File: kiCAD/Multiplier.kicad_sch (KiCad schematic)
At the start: 58 parts, among them IC2 ADG1221BRMZ, J1 Conn_01x02_Pin, J2 Conn_01x02_Pin, J3 Conn_01x02_Pin, Q7 Q_Dual_PNP_PNP_C1B1B2C2E2E1, Q8 Q_Dual_PNP_PNP_C1B1B2C2E2E1, U1 TS912, U10 TPS63060, U2 TLV340, U4 TS912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

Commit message: Initial routing and layout
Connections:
- net VCC: now also Q8.5 (E2); no longer Q7.5 (E2)
- net at Q7.6 (E1), Q8.1 (C1), Q8.2 (B1): now also Q8.3 (B2); no longer Q7.3 (B2)
- net at Q7.4 (C2): now also C1.1, U2.2 (-), U2.6 (-), U7.1; no longer Q8.5 (E2)
- net at Q7.1 (C1), Q7.2 (B1), R5.1: now also Q7.3 (B2); no longer Q8.3 (B2)
- new net: Q7.5 (E2), Q8.4 (C2)
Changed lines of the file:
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@@
-    )
-  )
-  (symbol (lib_id "Device:Q_Dual_PNP_PNP_C1B1B2C2E2E1") (at 76.2 27.94 0) (mirror x) (unit 2)
-    (in_bom yes) (on_board yes) (dnp no)
-    (property "Reference" "Q7" (at 81.28 26.67 0)
-      (effects (font (size 1.27 1.27)) (justify left))
-    )
-    (property "Value" "Q_Dual_PNP_PNP_C1B1B2C2E2E1" (at 81.28 29.21 0)
-      (effects (font (size 1.27 1.27)) (justify left) hide)
-    )
-    (property "Footprint" "Custom:SOT-363_DUAL_PNP" (at 81.28 30.48 0)
-      (effects (font (size 1.27 1.27)) hide)
-    )
-    (property "Datasheet" "https://www.diodes.com/assets/Datasheets/ds30437.pdf" (at 76.2 27.94 0)
-      (effects (font (size 1.27 1.27)) hide)
-    )
-    (pin "1")
-    (pin "2")
-    (pin "6")
-    (pin "3")
-    (pin "4")
-    (pin "5")
-    (instances
-      (project "Multiplier"
-        (path "/8f04f48d-7465-48f4-bbbe-36932343ce91"
-          (reference "Q7") (unit 2)
-        )
-      )
     )
   )
@@
     )
   )
-  (symbol (lib_id "Device:C") (at 83.82 78.74 0) (unit 1)
-    (in_bom yes) (on_board yes) (dnp no) (fields_autoplaced)
-    (property "Reference" "C1" (at 87.63 77.47 0)
-      (effects (font (size 1.27 1.27)) (justify left))
-    )
-    (property "Value" "1n" (at 87.63 80.01 0)
-      (effects (font (size 1.27 1.27)) (justify left))
-    )
-    (property "Footprint" "Resistor_SMD:R_0805_2012Metric_Pad1.20x1.40mm_HandSolder" (at 84.7852 82.55 0)
+  (symbol (lib_id "Device:C") (at 83.82 78.74 0) (mirror y) (unit 1)
+    (in_bom yes) (on_board yes) (dnp no)
+    (property "Reference" "C1" (at 80.01 77.47 0)
+      (effects (font (size 1.27 1.27)) (justify left))
+    )
+    (property "Value" "1n" (at 80.01 80.01 0)
+      (effects (font (size 1.27 1.27)) (justify left))
+    )
+    (property "Footprint" "Resistor_SMD:R_0805_2012Metric_Pad1.20x1.40mm_HandSolder" (at 82.8548 82.55 0)
       (effects (font (size 1.27 1.27)) hide)
     )
@@
     )
   )
+  (symbol (lib_id "Device:Q_Dual_PNP_PNP_C1B1B2C2E2E1") (at 76.2 27.94 0) (mirror x) (unit 2)
+    (in_bom yes) (on_board yes) (dnp no)
+    (property "Reference" "Q8" (at 81.28 26.67 0)
+      (effects (font (size 1.27 1.27)) (justify left))
+    )
+    (property "Value" "Q_Dual_PNP_PNP_C1B1B2C2E2E1" (at 81.28 29.21 0)
+      (effects (font (size 1.27 1.27)) (justify left) hide)
+    )
+    (property "Footprint" "Custom:SOT-363_DUAL_PNP" (at 81.28 30.48 0)
+      (effects (font (size 1.27 1.27)) hide)
+    )
+    (property "Datasheet" "https://www.diodes.com/assets/Datasheets/ds30437.pdf" (at 76.2 27.94 0)
+      (effects (font (size 1.27 1.27)) hide)
+    )
+    (pin "1")
+    (pin "2")
+    (pin "6")
+    (pin "3")
+    (pin "4")
+    (pin "5")
+    (instances
+      (project "Multiplier"
+        (path "/8f04f48d-7465-48f4-bbbe-36932343ce91"
+          (reference "Q8") (unit 2)
+        )
+      )
+    )
+  )
   (symbol (lib_id "Amplifier_Operational:TS912") (at 36.83 139.7 0) (unit 2)
     (in_bom yes) (on_board yes) (dnp no)
@@
     )
   )
-  (symbol (lib_id "Device:Q_Dual_PNP_PNP_C1B1B2C2E2E1") (at 76.2 40.64 0) (mirror x) (unit 2)
-    (in_bom yes) (on_board yes) (dnp no)
-    (property "Reference" "Q8" (at 81.28 39.37 0)
-      (effects (font (size 1.27 1.27)) (justify left))
-    )
-    (property "Value" "Q_Dual_PNP_PNP_C1B1B2C2E2E1" (at 81.28 41.91 0)
-      (effects (font (size 1.27 1.27)) (justify left) hide)
-    )
-    (property "Footprint" "Custom:SOT-363_DUAL_PNP" (at 81.28 43.18 0)
-      (effects (font (size 1.27 1.27)) hide)
-    )
-    (property "Datasheet" "https://www.diodes.com/assets/Datasheets/ds30437.pdf" (at 76.2 40.64 0)
-      (effects (font (size 1.27 1.27)) hide)
-    )
-    (pin "1")
-    (pin "2")
-    (pin "6")
-    (pin "3")
-    (pin "4")
-    (pin "5")
-    (instances
-      (project "Multiplier"
-        (path "/8f04f48d-7465-48f4-bbbe-36932343ce91"
-          (reference "Q8") (unit 2)
-        )
-      )
-    )
-  )
   (symbol (lib_id "Device:R") (at 59.69 180.34 90) (unit 1)
     (in_bom yes) (on_board yes) (dnp no)
@@
         )
       )
+    )
+  )
+  (symbol (lib_id "Device:Q_Dual_PNP_PNP_C1B1B2C2E2E1") (at 76.2 40.64 0) (mirror x) (unit 2)
+    (in_bom yes) (on_board yes) (dnp no)
+    (property "Reference" "Q7" (at 81.28 39.37 0)
+      (effects (font (size 1.27 1.27)) (justify left))
+    )
+    (property "Value" "Q_Dual_PNP_PNP_C1B1B2C2E2E1" (at 81.28 41.91 0)
+      (effects (font (size 1.27 1.27)) (justify left) hide)
+    )
+    (property "Footprint" "Custom:SOT-363_DUAL_PNP" (at 81.28 43.18 0)
+      (effects (font (size 1.27 1.27)) hide)
+    )
+    (property "Datasheet" "https://www.diodes.com/assets/Datasheets/ds30437.pdf" (at 76.2 40.64 0)
+      (effects (font (size 1.27 1.27)) hide)
+    )
+    (pin "1")
+    (pin "2")
+    (pin "6")
+    (pin "3")
+    (pin "4")
+    (pin "5")
+    (instances
+      (project "Multiplier"
+        (path "/8f04f48d-7465-48f4-bbbe-36932343ce91"
+          (reference "Q7") (unit 2)
+        )
+      )

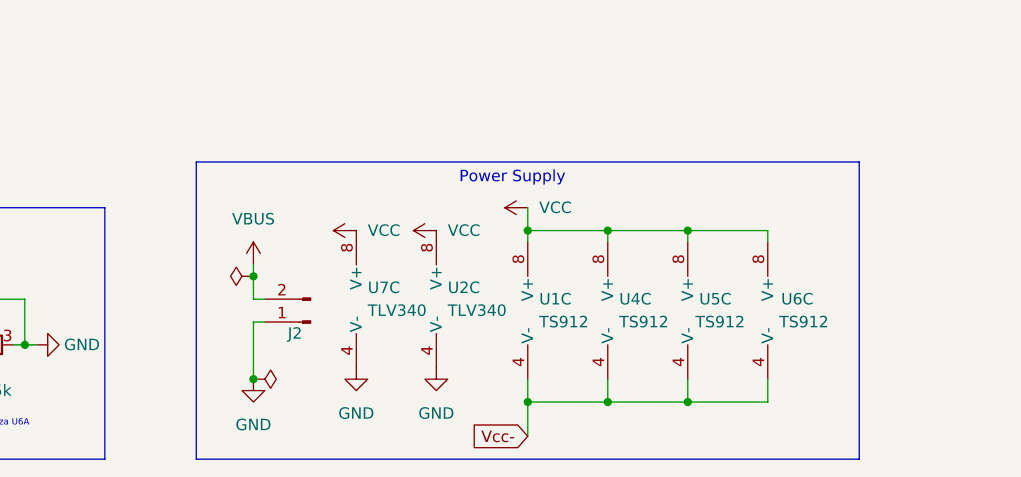
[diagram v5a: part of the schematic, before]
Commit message: First PCB design with GND fields and tantalum (100nF) coupling capacitor added
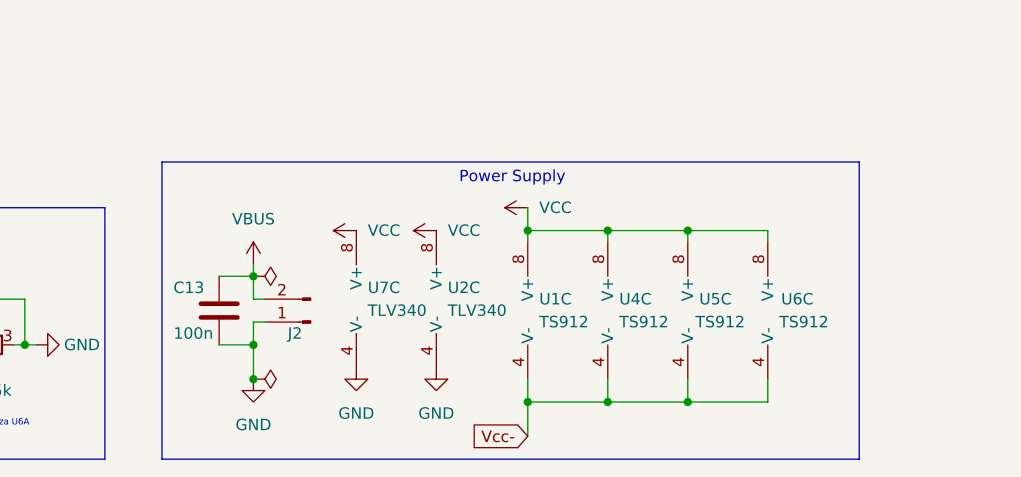
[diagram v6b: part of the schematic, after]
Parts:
- added C13: 100n, Custom:CAP_293D-B_VSS, symbol Device:C
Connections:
- net GND: now also C13.2
- net VBUS: now also C13.1
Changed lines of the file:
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@@
   (junction (at 273.05 115.57) (diameter 0) (color 0 0 0 0)
+  )
+  (junction (at 100.33 180.34) (diameter 0) (color 0 0 0 0)
   )
   (junction (at 148.59 186.69) (diameter 0) (color 0 0 0 0)
@@
     (stroke (width 0) (type default))
   )
-  (wire (pts (xy 100.33 177.8) (xy 100.33 184.15))
+  (wire (pts (xy 100.33 177.8) (xy 100.33 180.34))
     (stroke (width 0) (type default))
   )
@@
     (stroke (width 0) (type default))
   )
+  (wire (pts (xy 96.52 180.34) (xy 100.33 180.34))
+    (stroke (width 0) (type default))
+  )
   (wire (pts (xy 53.34 34.29) (xy 66.04 34.29))
     (stroke (width 0) (type default))
@@
     (stroke (width 0) (type default))
   )
+  (wire (pts (xy 96.52 172.72) (xy 100.33 172.72))
+    (stroke (width 0) (type default))
+  )
   (wire (pts (xy 143.51 36.83) (xy 143.51 39.37))
     (stroke (width 0) (type default))
@@
     (stroke (width 0) (type default))
   )
+  (wire (pts (xy 100.33 180.34) (xy 100.33 184.15))
+    (stroke (width 0) (type default))
+  )
   (wire (pts (xy 83.82 73.66) (xy 83.82 74.93))
     (stroke (width 0) (type default))
@@
     (fill (type none))
   )
-  (rectangle (start 93.98 160.02) (end 167.64 193.04)
+  (rectangle (start 90.17 160.02) (end 167.64 193.04)
     (stroke (width 0) (type default))
     (fill (type none))
@@
     )
   )
-  (symbol (lib_id "power:PWR_FLAG") (at 100.33 172.72 90) (unit 1)
-    (in_bom yes) (on_board yes) (dnp no) (fields_autoplaced)
-    (property "Reference" "#FLG01" (at 98.425 172.72 0)
-      (effects (font (size 1.27 1.27)) hide)
-    )
-    (property "Value" "PWR_FLAG" (at 96.52 172.72 90)
+  (symbol (lib_id "power:PWR_FLAG") (at 100.33 172.72 270) (mirror x) (unit 1)
+    (in_bom yes) (on_board yes) (dnp no)
+    (property "Reference" "#FLG01" (at 102.235 172.72 0)
+      (effects (font (size 1.27 1.27)) hide)
+    )
+    (property "Value" "PWR_FLAG" (at 104.14 172.72 90)
       (effects (font (size 1.27 1.27)) (justify left) hide)
     )
@@
         )
       )
+    )
+  )
+  (symbol (lib_id "Device:C") (at 96.52 176.53 0) (unit 1)
+    (in_bom yes) (on_board yes) (dnp no)
+    (property "Reference" "C13" (at 91.44 173.99 0)
+      (effects (font (size 1.27 1.27)) (justify left))
+    )
+    (property "Value" "100n" (at 91.44 179.07 0)
+      (effects (font (size 1.27 1.27)) (justify left))
+    )
+    (property "Footprint" "Custom:CAP_293D-B_VSS" (at 97.4852 180.34 0)
+      (effects (font (size 1.27 1.27)) hide)
+    )
+    (property "Datasheet" "~" (at 96.52 176.53 0)
+      (effects (font (size 1.27 1.27)) hide)
+    )
+    (pin "1")
+    (pin "2")
+    (instances
+      (project "Multiplier"
+        (path "/8f04f48d-7465-48f4-bbbe-36932343ce91"
+          (reference "C13") (unit 1)
+        )
+      )

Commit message: New schematic image, final PCB design
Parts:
- added C14, C15, C16, C17, C18, C19, C20, C21, C22: 100n, Capacitor_SMD:C_0805_2012Metric, symbol Device:C
- C1: footprint Resistor_SMD:R_0805_2012Metric_Pad1.20x1.40mm_HandSolder -> Capacitor_SMD:C_0805_2012Metric
- C13: value 100n -> 100u
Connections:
- net GND: now also C14.2, C15.2, C16.2, C21.2, C22.2
- net VCC: now also C14.1, C15.1, C16.1, C17.1, C18.1, C19.1, C20.1, C21.1, C22.1
- net Vcc-: now also C17.2, C18.2, C19.2, C20.2
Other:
- moved on the sheet: C5
